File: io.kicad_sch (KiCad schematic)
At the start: 8 parts, among them J10 Conn_01x14, J3 Conn_01x38, J4 Conn_01x22, J5 Conn_02x11, J6 Conn_01x38, J7 Conn_01x38, J8 Conn_01x38, J9 Conn_01x14

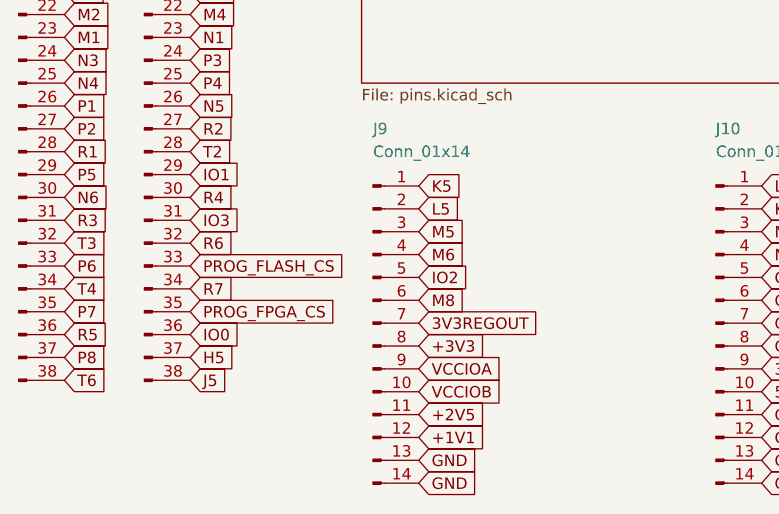
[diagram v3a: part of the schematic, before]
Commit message: Route power, FTDI chip
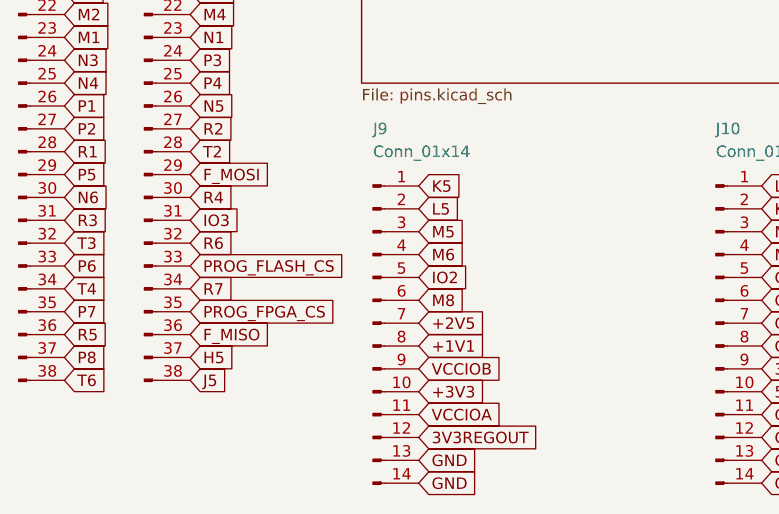
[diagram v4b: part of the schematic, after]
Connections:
- net +1V1: now also J9.8 (Pin_8); no longer J9.12 (Pin_12)
- net +2V5: now also J9.7 (Pin_7); no longer J9.11 (Pin_11)
- net +3V3: now also J9.10 (Pin_10); no longer J9.8 (Pin_8)
- net 3V3REGOUT: now also J9.12 (Pin_12); no longer J9.7 (Pin_7)
- net VCCIOA: now also J9.11 (Pin_11); no longer J9.9 (Pin_9)
- net VCCIOB: now also J9.9 (Pin_9); no longer J9.10 (Pin_10)
- net IO0 renamed F_MISO
- net IO1 renamed F_MOSI
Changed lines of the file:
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@@
+    )
+  )
+  (global_label "+1V1" (shape input) (at 74.93 144.78 0) (fields_autoplaced)
+    (effects (font (size 1.27 1.27)) (justify left))
+    (property "Intersheetrefs" "${INTERSHEET_REFS}" (at 82.9158 144.78 0)
+      (effects (font (size 1.27 1.27)) (justify left) hide)
     )
   )
@@
     )
   )
+  (global_label "VCCIOA" (shape input) (at 74.93 152.4 0) (fields_autoplaced)
+    (effects (font (size 1.27 1.27)) (justify left))
+    (property "Intersheetrefs" "${INTERSHEET_REFS}" (at 84.4883 152.4 0)
+      (effects (font (size 1.27 1.27)) (justify left) hide)
+    )
+  )
   (global_label "A15" (shape input) (at 140.97 55.88 0) (fields_autoplaced)
     (effects (font (size 1.27 1.27)) (justify left))
@@
     )
   )
+  (global_label "VCCIOB" (shape input) (at 74.93 147.32 0) (fields_autoplaced)
+    (effects (font (size 1.27 1.27)) (justify left))
+    (property "Intersheetrefs" "${INTERSHEET_REFS}" (at 84.6697 147.32 0)
+      (effects (font (size 1.27 1.27)) (justify left) hide)
+    )
+  )
   (global_label "G1" (shape input) (at 49.53 87.63 0) (fields_autoplaced)
     (effects (font (size 1.27 1.27)) (justify left))
@@
     )
   )
-  (global_label "IO1" (shape input) (at 49.53 125.73 0) (fields_autoplaced)
-    (effects (font (size 1.27 1.27)) (justify left))
-    (property "Intersheetrefs" "${INTERSHEET_REFS}" (at 55.5806 125.73 0)
-      (effects (font (size 1.27 1.27)) (justify left) hide)
-    )
-  )
   (global_label "C13" (shape input) (at 161.29 60.96 0) (fields_autoplaced)
     (effects (font (size 1.27 1.27)) (justify left))
@@
     )
   )
-  (global_label "3V3REGOUT" (shape input) (at 74.93 142.24 0) (fields_autoplaced)
-    (effects (font (size 1.27 1.27)) (justify left))
-    (property "Intersheetrefs" "${INTERSHEET_REFS}" (at 88.661 142.24 0)
-      (effects (font (size 1.27 1.27)) (justify left) hide)
-    )
-  )
   (global_label "P2" (shape input) (at 35.56 120.65 0) (fields_autoplaced)
     (effects (font (size 1.27 1.27)) (justify left))
@@
     )
   )
+  (global_label "F_MOSI" (shape input) (at 49.53 125.73 0) (fields_autoplaced)
+    (effects (font (size 1.27 1.27)) (justify left))
+    (property "Intersheetrefs" "${INTERSHEET_REFS}" (at 59.0882 125.73 0)
+      (effects (font (size 1.27 1.27)) (justify left) hide)
+    )
+  )
   (global_label "M8" (shape input) (at 74.93 139.7 0) (fields_autoplaced)
     (effects (font (size 1.27 1.27)) (justify left))
@@
     )
   )
-  (global_label "+2V5" (shape input) (at 74.93 152.4 0) (fields_autoplaced)
-    (effects (font (size 1.27 1.27)) (justify left))
-    (property "Intersheetrefs" "${INTERSHEET_REFS}" (at 82.9158 152.4 0)
-      (effects (font (size 1.27 1.27)) (justify left) hide)
-    )
-  )
   (global_label "A11" (shape input) (at 105.41 41.91 270) (fields_autoplaced)
     (effects (font (size 1.27 1.27)) (justify right))
@@
     )
   )
+  (global_label "+2V5" (shape input) (at 74.93 142.24 0) (fields_autoplaced)
+    (effects (font (size 1.27 1.27)) (justify left))
+    (property "Intersheetrefs" "${INTERSHEET_REFS}" (at 82.9158 142.24 0)
+      (effects (font (size 1.27 1.27)) (justify left) hide)
+    )
+  )
   (global_label "P12" (shape input) (at 161.29 127 0) (fields_autoplaced)
     (effects (font (size 1.27 1.27)) (justify left))
@@
     )
   )
-  (global_label "+3V3" (shape input) (at 74.93 144.78 0) (fields_autoplaced)
-    (effects (font (size 1.27 1.27)) (justify left))
-    (property "Intersheetrefs" "${INTERSHEET_REFS}" (at 82.9158 144.78 0)
-      (effects (font (size 1.27 1.27)) (justify left) hide)
-    )
-  )
-  (global_label "IO0" (shape input) (at 49.53 143.51 0) (fields_autoplaced)
-    (effects (font (size 1.27 1.27)) (justify left))
-    (property "Intersheetrefs" "${INTERSHEET_REFS}" (at 55.5806 143.51 0)
-      (effects (font (size 1.27 1.27)) (justify left) hide)
-    )
-  )
   (global_label "K16" (shape input) (at 140.97 96.52 0) (fields_autoplaced)
     (effects (font (size 1.27 1.27)) (justify left))
@@
     )
   )
-  (global_label "VCCIOA" (shape input) (at 74.93 147.32 0) (fields_autoplaced)
-    (effects (font (size 1.27 1.27)) (justify left))
-    (property "Intersheetrefs" "${INTERSHEET_REFS}" (at 84.4883 147.32 0)
-      (effects (font (size 1.27 1.27)) (justify left) hide)
-    )
-  )
-  (global_label "+1V1" (shape input) (at 74.93 154.94 0) (fields_autoplaced)
-    (effects (font (size 1.27 1.27)) (justify left))
-    (property "Intersheetrefs" "${INTERSHEET_REFS}" (at 82.9158 154.94 0)
+  (global_label "F_MISO" (shape input) (at 49.53 143.51 0) (fields_autoplaced)
+    (effects (font (size 1.27 1.27)) (justify left))
+    (property "Intersheetrefs" "${INTERSHEET_REFS}" (at 59.0882 143.51 0)
       (effects (font (size 1.27 1.27)) (justify left) hide)
     )
@@
     )
   )
-  (global_label "VCCIOB" (shape input) (at 74.93 149.86 0) (fields_autoplaced)
-    (effects (font (size 1.27 1.27)) (justify left))
-    (property "Intersheetrefs" "${INTERSHEET_REFS}" (at 84.6697 149.86 0)
-      (effects (font (size 1.27 1.27)) (justify left) hide)
-    )
-  )
   (global_label "B7" (shape input) (at 87.63 41.91 270) (fields_autoplaced)
     (effects (font (size 1.27 1.27)) (justify right))
@@
     )
   )
+  (global_label "+3V3" (shape input) (at 74.93 149.86 0) (fields_autoplaced)
+    (effects (font (size 1.27 1.27)) (justify left))
+    (property "Intersheetrefs" "${INTERSHEET_REFS}" (at 82.9158 149.86 0)
+      (effects (font (size 1.27 1.27)) (justify left) hide)
+    )
+  )
   (global_label "GND" (shape input) (at 113.03 142.24 0) (fields_autoplaced)
     (effects (font (size 1.27 1.27)) (justify left))
@@
       (effects (font (size 1.27 1.27)) (justify left) hide)
     )
+  )
+  (global_label "3V3REGOUT" (shape input) (at 74.93 154.94 0) (fields_autoplaced)
+    (effects (font (size 1.27 1.27)) (justify left))
+    (property "Intersheetrefs" "${INTERSHEET_REFS}" (at 88.661 154.94 0)
+      (effects (font (size 1.27 1.27)) (justify left) hide)
+    )
